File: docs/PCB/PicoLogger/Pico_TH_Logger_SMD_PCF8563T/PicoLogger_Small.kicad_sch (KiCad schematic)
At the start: 27 parts, among them J1 Sensor, J2 LCD 16x2, J3 Additional connector, J5 SPI, SW1 SW_Push, SW2 SW_Push, U1 PCF8563T, Y1 Crystal

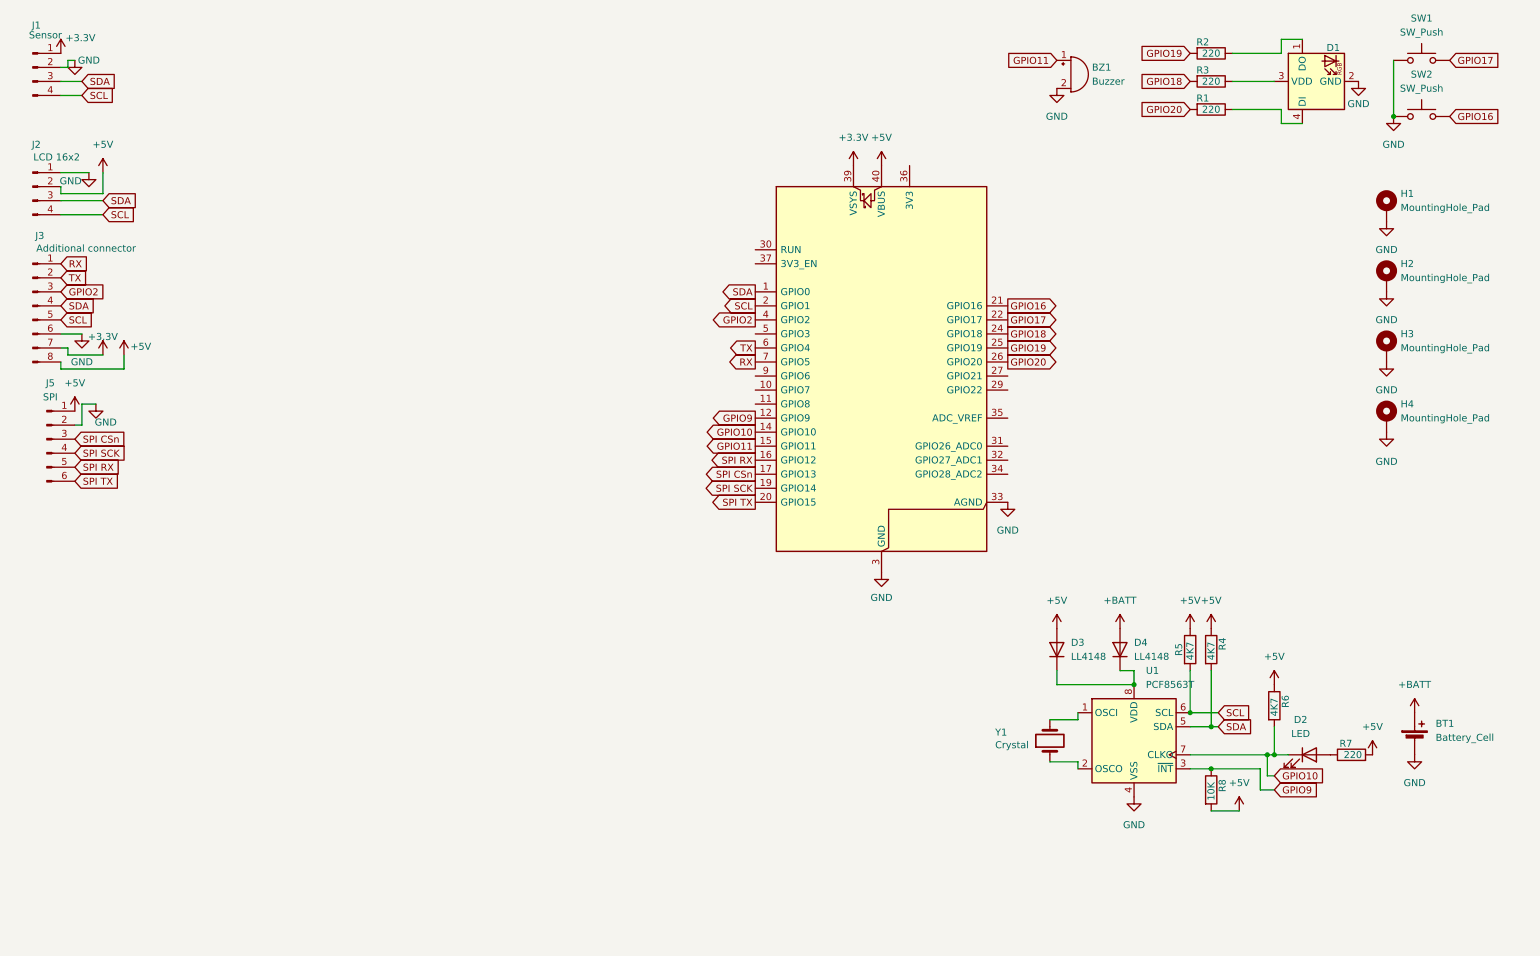
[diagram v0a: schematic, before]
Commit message: Logger docs updated.
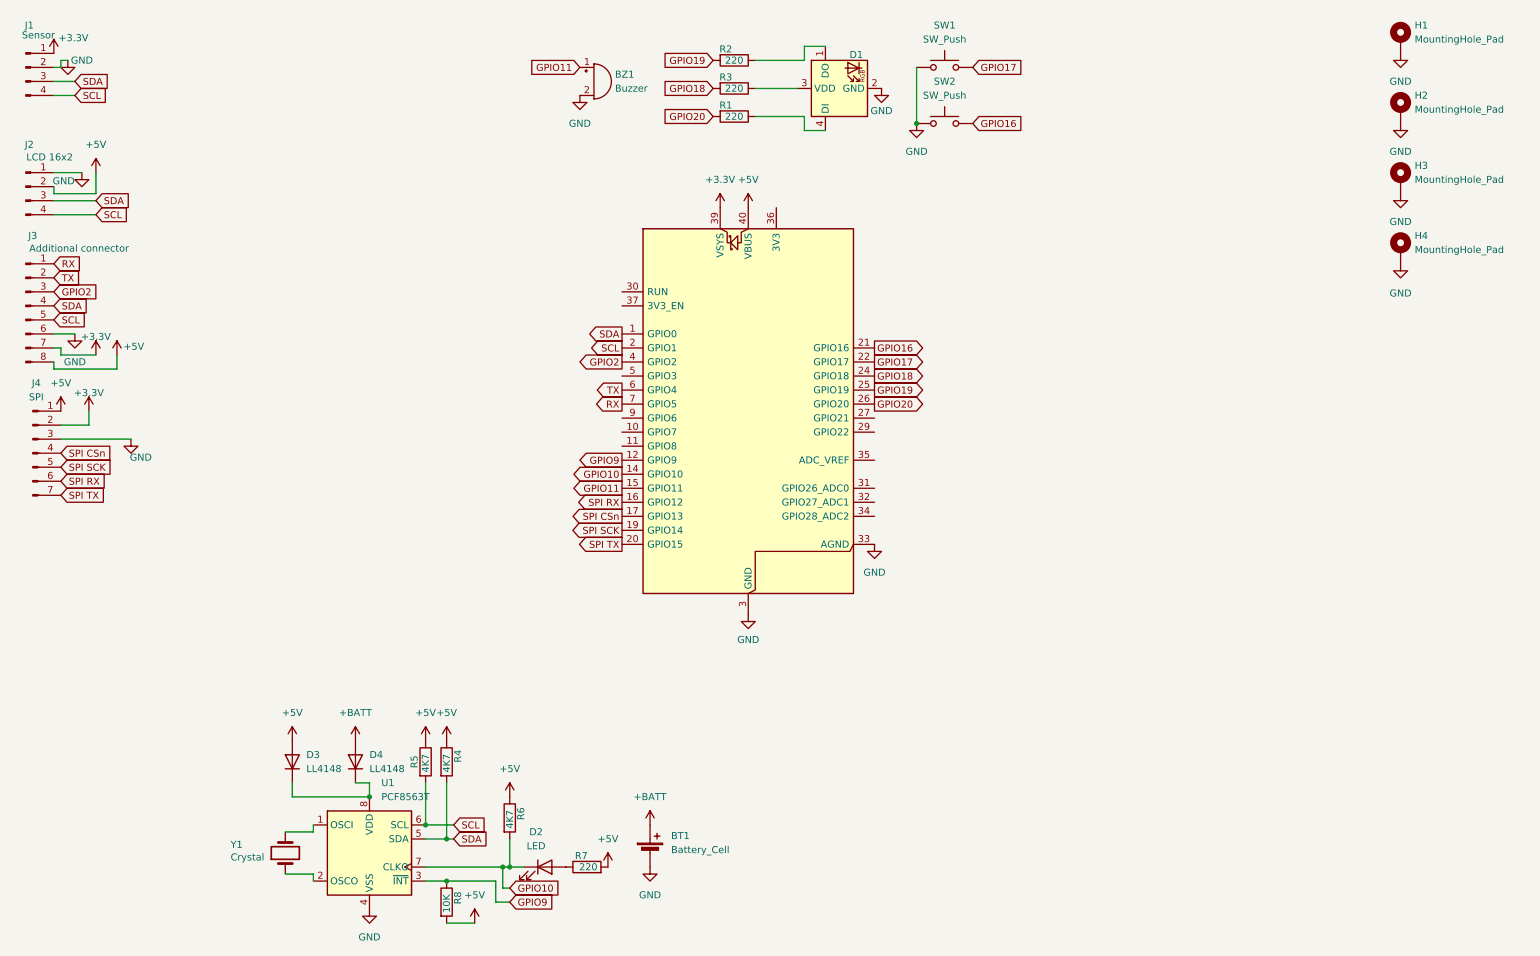
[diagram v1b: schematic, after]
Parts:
- removed J5: SPI, Connector_PinHeader_2.54mm:PinHeader_1x06_P2.54mm_Horizontal, symbol Connector:Conn_01x06_Pin
- added J4: SPI, Connector_PinHeader_2.54mm:PinHeader_1x07_P2.54mm_Horizontal, symbol Connector:Conn_01x07_Pin
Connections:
- net +3.3V: now also J4.2 (Pin_2)
- net +5V: now also J4.1 (Pin_1)
- net GND: now also J4.3 (Pin_3)
- net SPI CSn: now also J4.4 (Pin_4)
- net SPI RX: now also J4.6 (Pin_6)
- net SPI SCK: now also J4.5 (Pin_5)
- net SPI TX: now also J4.7 (Pin_7)
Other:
- company: (none) -> Creator: Piotr Kłyś
- title: (none) -> Raspberry Pi Pico Logger
- moved on the sheet: BT1, BZ1, D1, D2, D3, D4, H1, H2, H3, H4, J1, J2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

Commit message: Updated docs.
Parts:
- removed BT1: Battery_Cell, Battery:BatteryHolder_Keystone_104_1x23mm, symbol Device:Battery_Cell
- removed BZ1: Buzzer, Buzzer_Beeper:Buzzer_12x9.5RM7.6, symbol Device:Buzzer
- removed D1: APA-106-F5, LED_SMD:LED_Avago_PLCC4_3.2x2.8mm_CW, symbol LED:APA-106-F5
- removed D2: LED, LED_SMD:LED_0805_2012Metric, symbol Device:LED
- removed D3, D4: LL4148, Diode_SMD:D_MiniMELF, symbol Diode:LL4148
- removed J1: Sensor, Connector_PinHeader_2.54mm:PinHeader_1x04_P2.54mm_Vertical, symbol Connector:Conn_01x04_Pin
- removed J2: LCD 16x2, Connector_PinHeader_2.54mm:PinHeader_1x04_P2.54mm_Vertical, symbol Connector:Conn_01x04_Pin
- removed J3: Additional connector, Connector_PinHeader_2.54mm:PinHeader_1x08_P2.54mm_Horizontal, symbol Connector:Conn_01x08_Pin
- removed J4: SPI, Connector_PinHeader_2.54mm:PinHeader_1x07_P2.54mm_Horizontal, symbol Connector:Conn_01x07_Pin
- removed R1, R2, R3, R7: 220, Resistor_SMD:R_0805_2012Metric, symbol Device:R
- removed R4, R5, R6: 4K7, Resistor_SMD:R_0805_2012Metric, symbol Device:R
- removed R8: 10K, Resistor_SMD:R_0805_2012Metric, symbol Device:R
- removed SW1, SW2: SW_Push, Button_Switch_THT:SW_PUSH_6mm, symbol Switch:SW_Push
- removed U1: PCF8563T, Package_SO:SOIC-8_3.9x4.9mm_P1.27mm, symbol Timer_RTC:PCF8563T
- removed Y1: Crystal, Crystal:Crystal_SMD_3215-2Pin_3.2x1.5mm, symbol Device:Crystal
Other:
- added sheet connectors (connectors.kicad_sch)
- added sheet peripherals (peripherals.kicad_sch)
- added sheet rtc (rtc.kicad_sch)
- moved on the sheet: H1, H2, H3, H4
